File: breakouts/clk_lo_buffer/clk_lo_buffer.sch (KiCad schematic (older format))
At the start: 40 parts, among them U101 CONN_SMA_2GND, U102 NB3N551, U103 CONN_SMA_2GND, U104 CONN_SMA_2GND, U105 CONN_SMA_2GND, U106 CONN_SMA_2GND, U107 CONN_SMA_2GND, U108 MMG3012NT1, U109 CONN_SMA_2GND, U110 CONN_SMA_2GND, U111 CONN_SMA_2GND, U112 CONN_SMA_2GND

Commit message: finished and ordered clk/lo buffer for demod board
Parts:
- added H101, H102, H103, H104: MOUNTING_HOLE, Mounting_Holes:MountingHole_2-7mm, symbol MOUNTING_HOLE
- D101: renamed from D?; footprint (none) -> LEDs:LED_0603
- P101: renamed from P?; footprint (none) -> Terminal_Blocks:TerminalBlock_Pheonix_PT-3.5mm_2pol
- R118: renamed from R?; footprint (none) -> Resistors_SMD:R_0603
- gave numbers to parts that had none: 1
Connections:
- net CLK1: now reaches R108.2, U102.2 (Q1), U105.1 (RF)
- net CLK2: now reaches R107.2, U102.3 (Q2), U104.1 (RF)
- net CLK3: now reaches R110.2, U102.4 (Q3), U107.1 (RF)
- net CLK4: now reaches R109.2, U102.5 (Q4), U106.1 (RF)
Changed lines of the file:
@@
 LIBS:hmc475
 LIBS:nb3n551
+LIBS:mounting_hole
 LIBS:clk_lo_buffer-cache
 EELAYER 25 0
@@
 Connection ~ 1200 6050
 $Comp
-L CONN_01X02 P?
+L CONN_01X02 P101
 U 1 1 580F5B09
 P 2950 1550
-F 0 "P?" H 2950 1700 50  0000 C CNN
+F 0 "P101" H 2950 1700 50  0000 C CNN
 F 1 "CONN_01X02" V 3050 1550 50  0000 C CNN
-F 2 "" H 2950 1550 50  0000 C CNN
+F 2 "Terminal_Blocks:TerminalBlock_Pheonix_PT-3.5mm_2pol" H 2950 1550 50  0001 C CNN
 F 3 "" H 2950 1550 50  0000 C CNN
 	1    2950 1550
@@
 $EndComp
 $Comp
-L +5V #PWR?
+L +5V #PWR027
 U 1 1 580F5B8B
 P 2400 1250
-F 0 "#PWR?" H 2400 1100 50  0001 C CNN
+F 0 "#PWR027" H 2400 1100 50  0001 C CNN
 F 1 "+5V" H 2400 1390 50  0000 C CNN
 F 2 "" H 2400 1250 50  0000 C CNN
@@
 	1950 1500 2750 1500
 $Comp
-L GND #PWR?
+L GND #PWR028
 U 1 1 580F5EDE
 P 2650 1900
-F 0 "#PWR?" H 2650 1650 50  0001 C CNN
+F 0 "#PWR028" H 2650 1650 50  0001 C CNN
 F 1 "GND" H 2650 1750 50  0000 C CNN
 F 2 "" H 2650 1900 50  0000 C CNN
@@
 	2650 1600 2650 1900
 $Comp
-L C_Small C?
+L C_Small C107
 U 1 1 580F6211
 P 2400 1750
-F 0 "C?" H 2410 1820 50  0000 L CNN
+F 0 "C107" H 2410 1820 50  0000 L CNN
 F 1 "10 uF" H 2410 1670 50  0000 L CNN
 F 2 "Capacitors_SMD:C_0603" H 2400 1750 50  0001 C CNN
@@
 $EndComp
 $Comp
-L GND #PWR?
+L GND #PWR029
 U 1 1 580F644A
 P 2400 1900
-F 0 "#PWR?" H 2400 1650 50  0001 C CNN
+F 0 "#PWR029" H 2400 1650 50  0001 C CNN
 F 1 "GND" H 2400 1750 50  0000 C CNN
 F 2 "" H 2400 1900 50  0000 C CNN
@@
 Connection ~ 2400 1500
 $Comp
-L R_Small R?
+L R_Small R118
 U 1 1 580F66A2
 P 1950 1700
-F 0 "R?" H 1980 1720 50  0000 L CNN
+F 0 "R118" H 1980 1720 50  0000 L CNN
 F 1 "10k" H 1980 1660 50  0000 L CNN
-F 2 "" H 1950 1700 50  0000 C CNN
+F 2 "Resistors_SMD:R_0603" H 1950 1700 50  0001 C CNN
 F 3 "" H 1950 1700 50  0000 C CNN
 	1    1950 1700
@@
 $EndComp
 $Comp
-L LED D?
+L LED D101
 U 1 1 580F681F
 P 1950 2050
-F 0 "D?" H 1950 2150 50  0000 C CNN
+F 0 "D101" H 1950 2150 50  0000 C CNN
 F 1 "LED" H 1950 1950 50  0000 C CNN
-F 2 "" H 1950 2050 50  0000 C CNN
+F 2 "LEDs:LED_0603" H 1950 2050 50  0001 C CNN
 F 3 "" H 1950 2050 50  0000 C CNN
 	1    1950 2050
@@
 $EndComp
 $Comp
-L GND #PWR?
+L GND #PWR030
 U 1 1 580F6FE5
 P 1950 2350
-F 0 "#PWR?" H 1950 2100 50  0001 C CNN
+F 0 "#PWR030" H 1950 2100 50  0001 C CNN
 F 1 "GND" H 1950 2200 50  0000 C CNN
 F 2 "" H 1950 2350 50  0000 C CNN
@@
 Wire Wire Line
 	1950 1500 1950 1600
+$Comp
+L MOUNTING_HOLE H101
+U 1 1 580F7BD8
+P 3100 3600
+F 0 "H101" H 2800 3650 60  0000 C CNN
+F 1 "MOUNTING_HOLE" H 3100 3750 60  0000 C CNN
+F 2 "Mounting_Holes:MountingHole_2-7mm" H 3100 3600 60  0001 C CNN
+F 3 "" H 3100 3600 60  0000 C CNN
+	1    3100 3600
+	1    0    0    -1
+$EndComp
+$Comp
+L MOUNTING_HOLE H102
+U 1 1 580F7C66
+P 3100 3900
+F 0 "H102" H 2800 3950 60  0000 C CNN
+F 1 "MOUNTING_HOLE" H 3100 4050 60  0000 C CNN
+F 2 "Mounting_Holes:MountingHole_2-7mm" H 3100 3900 60  0001 C CNN
+F 3 "" H 3100 3900 60  0000 C CNN
+	1    3100 3900
+	1    0    0    -1
+$EndComp
+$Comp
+L MOUNTING_HOLE H103
+U 1 1 580F7D0C
+P 3100 4200
+F 0 "H103" H 2800 4250 60  0000 C CNN
+F 1 "MOUNTING_HOLE" H 3100 4350 60  0000 C CNN
+F 2 "Mounting_Holes:MountingHole_2-7mm" H 3100 4200 60  0001 C CNN
+F 3 "" H 3100 4200 60  0000 C CNN
+	1    3100 4200
+	1    0    0    -1
+$EndComp
+$Comp
+L MOUNTING_HOLE H104
+U 1 1 580F7DA9
+P 3100 4500
+F 0 "H104" H 2800 4550 60  0000 C CNN
+F 1 "MOUNTING_HOLE" H 3100 4650 60  0000 C CNN
+F 2 "Mounting_Holes:MountingHole_2-7mm" H 3100 4500 60  0001 C CNN
+F 3 "" H 3100 4500 60  0000 C CNN
+	1    3100 4500
+	1    0    0    -1
+$EndComp
+Text Label 4550 5850 0    60   ~ 0
+CLK4
+Text Label 4550 6050 0    60   ~ 0
+CLK3
+Text Label 4550 6200 0    60   ~ 0
+CLK2
+Text Label 4550 6800 0    60   ~ 0
+CLK1
 $EndSCHEMATC

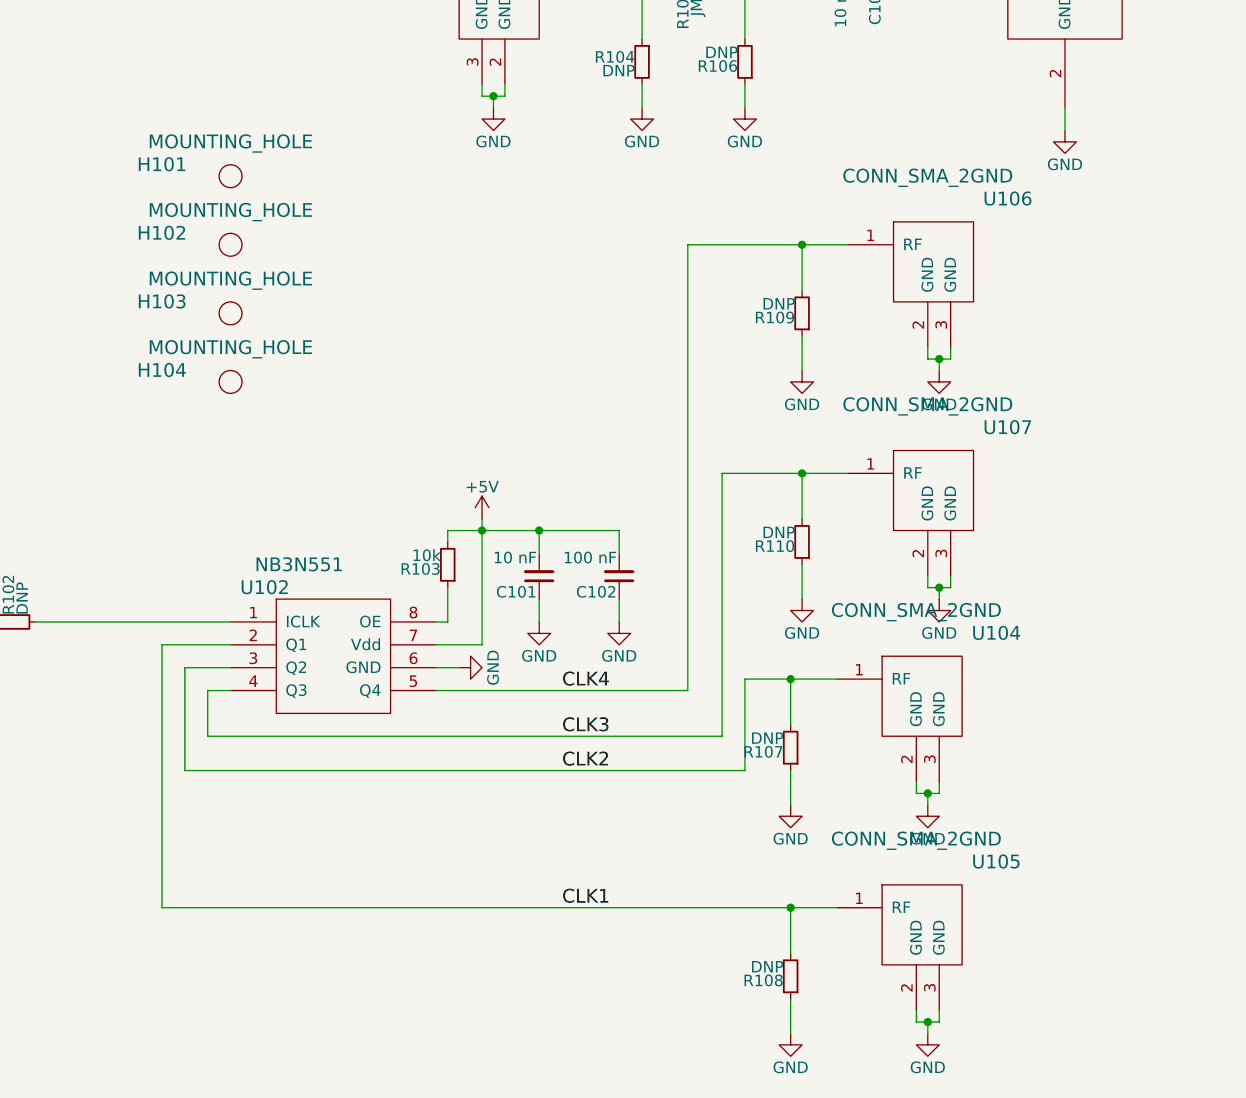
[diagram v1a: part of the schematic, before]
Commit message: added divider to output of clock buffer to avoid overloading adc fref...
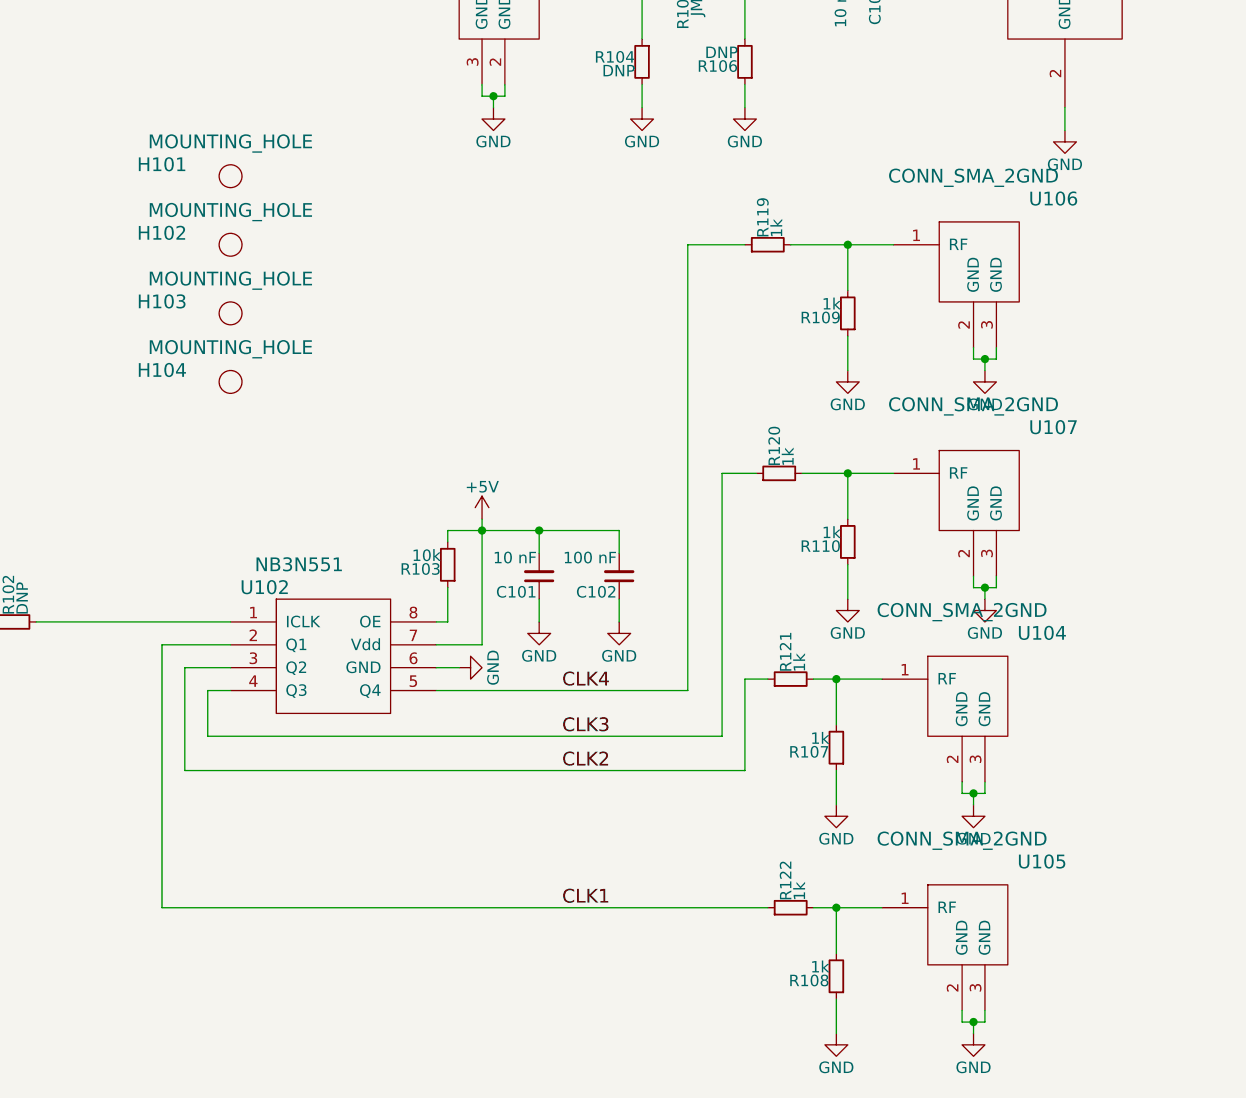
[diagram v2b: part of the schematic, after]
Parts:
- added R119, R120, R121, R122: 1k, Resistors_SMD:R_0603, symbol R_Small
- R107, R108, R109, R110: value DNP -> 1k
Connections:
- net CLK1: now also R122.1; no longer R108.2, U105.1 (RF)
- net CLK2: now also R121.1; no longer R107.2, U104.1 (RF)
- net CLK3: now also R120.1; no longer R110.2, U107.1 (RF)
- net CLK4: now also R119.1; no longer R109.2, U106.1 (RF)
- new net: R108.2, R122.2, U105.1 (RF)
- new net: R107.2, R121.2, U104.1 (RF)
- new net: R110.2, R120.2, U107.1 (RF)
- new net: R109.2, R119.2, U106.1 (RF)
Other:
- moved on the sheet: R107, R108, R109, R110, U104, U105, U106, U107
